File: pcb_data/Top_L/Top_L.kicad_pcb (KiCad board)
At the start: 2 copper layers, 158.4 x 96.4 mm, 75 parts, among them U1 XIAO-nRF52840

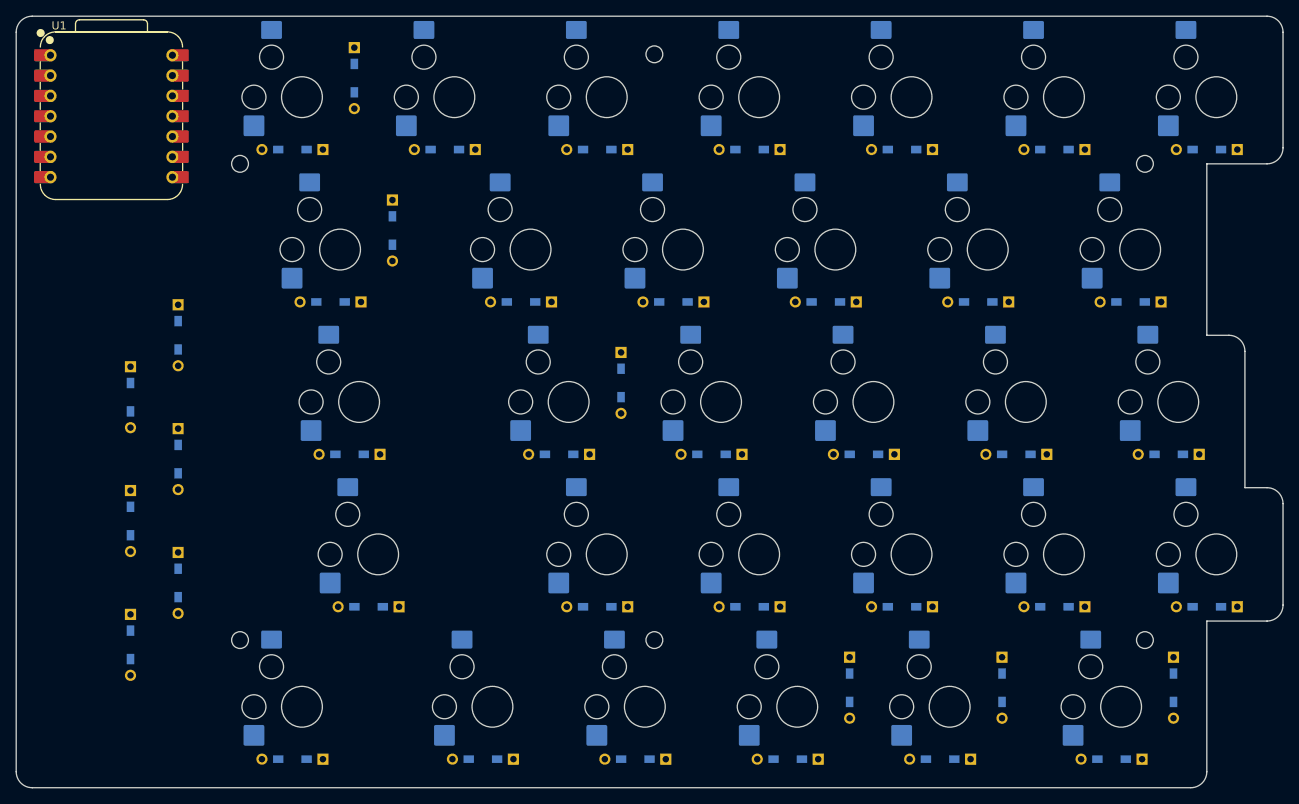
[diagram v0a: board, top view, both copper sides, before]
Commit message: remove diode
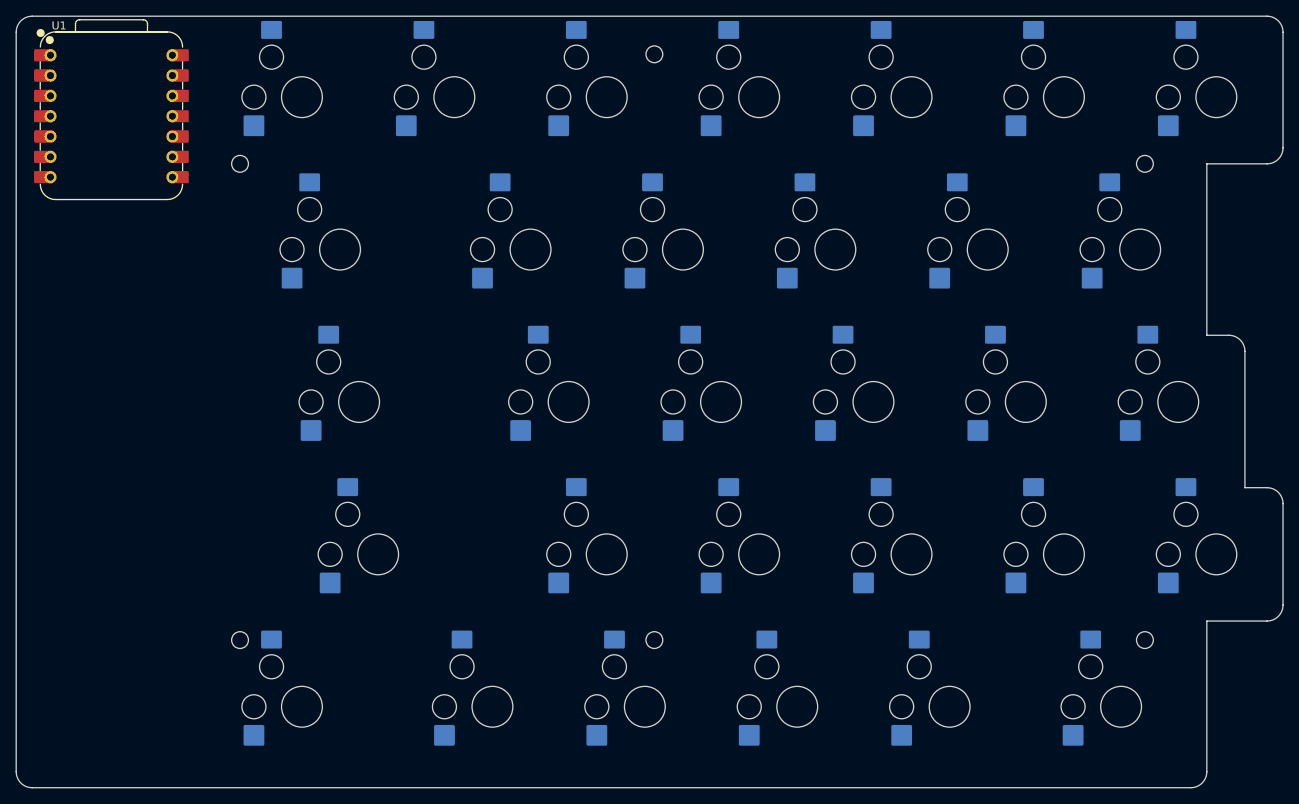
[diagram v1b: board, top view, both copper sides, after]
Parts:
- removed D0-1, D0-2, D0-3, D0-4, D1-0, D1-2, D1-3, D1-4, D2-0, D2-1, D2-3, D2-4, D3-0, D3-1, D3-2, D3-4, D4-0, D4-1, D4-2, D4-3, D5-0, D5-1, D5-2, D5-3, D5-4, D6-0, D6-1, D6-2, D6-3, D6-4, D6-5, DI0, DI1, DI2, DI3, DI4, DI5, DS0, DS1, DS2, DS3, DS4, DS5: 1N4148W, kbd_Parts:Diode_TH_SMD

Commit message: replace fp
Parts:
- RC0-1: footprint custom-library:Kailh-PG1353-Hotswap-L-1.5U -> kbd_SW_Hole:SW_Hole_1.5u
- RC0-2: footprint custom-library:Kailh-PG1353-Hotswap-L-1.75U -> kbd_SW_Hole:SW_Hole_1.75u
- RC0-3: footprint custom-library:Kailh-PG1353-Hotswap-L-2U -> kbd_SW_Hole:SW_Hole_2u
- RC6-5: footprint custom-library:Kailh-PG1353-Hotswap-L-1.25U -> kbd_SW_Hole:SW_Hole_1.25u
- turned RC0-3 to 180 degrees

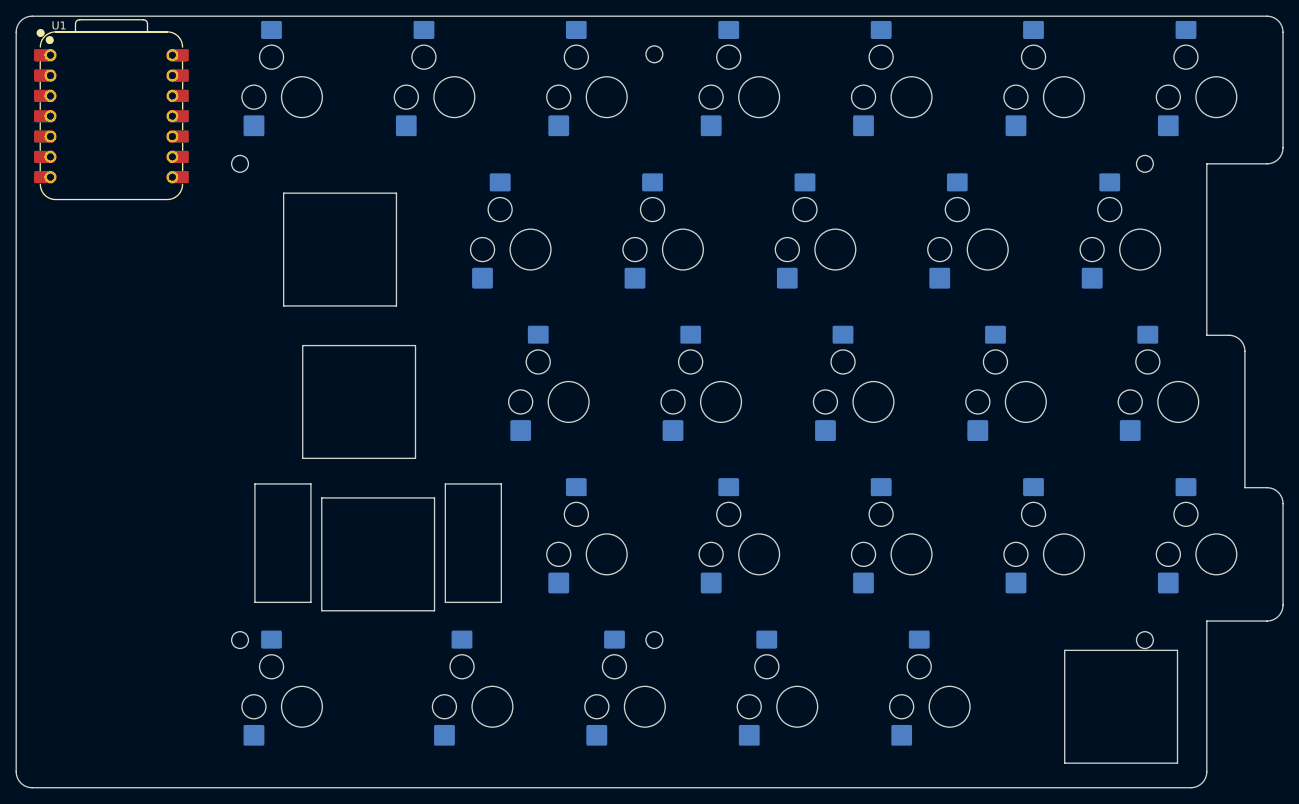
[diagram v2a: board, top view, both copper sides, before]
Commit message: replace fp
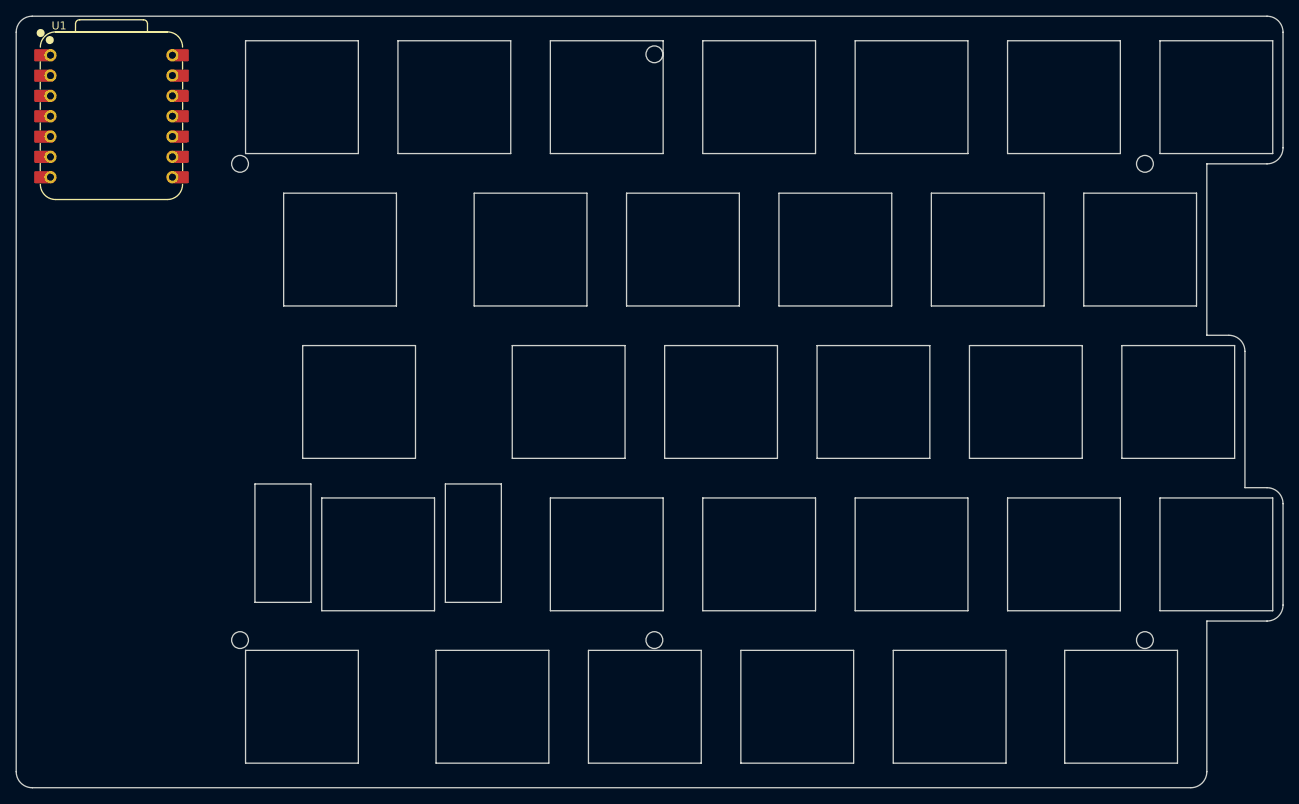
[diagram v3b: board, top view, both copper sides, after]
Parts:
- RC0-4, RC1-0, RC1-2, RC1-3, RC1-4, RC2-0, RC2-1, RC2-3, RC2-4, RC3-0, RC3-1, RC3-2, RC3-4, RC4-0, RC4-1, RC4-2, RC4-3, RC5-0, RC5-1, RC5-2, RC5-3, RC5-4, RC6-0, RC6-1, RC6-2, RC6-3, RC6-4: footprint custom-library:Kailh-PG1353-Hotswap-L-1U -> kbd_SW_Hole:SW_Hole_1u

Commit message: replace fp (m2 screw hole)
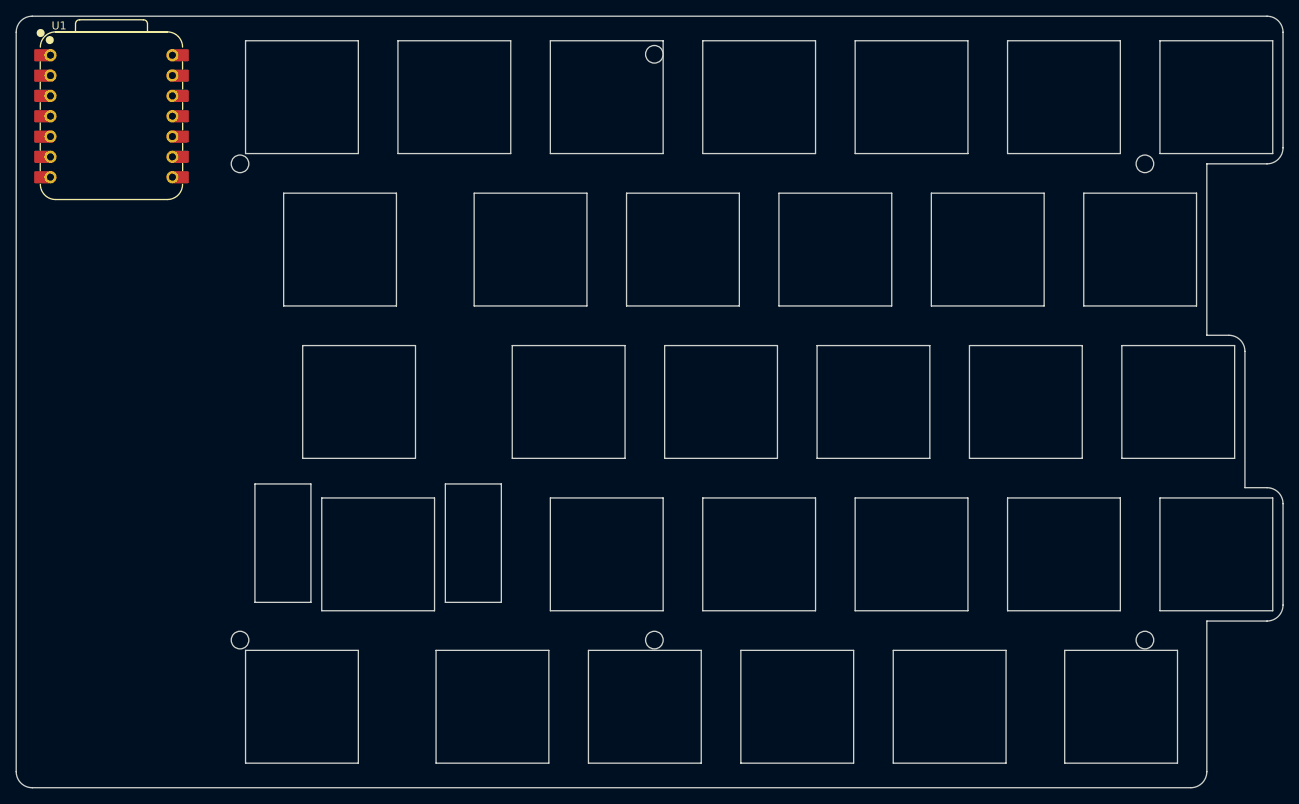
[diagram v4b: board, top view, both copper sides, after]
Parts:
- added Ref**: Val**, kbd_Hole:m2_Screw_Hole, F.Cu at (125.0, 125.0)
- added Ref**: Val**, kbd_Hole:m2_Screw_Hole, F.Cu at (125.0, 51.8)
- added Ref**: Val**, kbd_Hole:m2_Screw_Hole, F.Cu at (186.3, 65.5)
- added Ref**: Val**, kbd_Hole:m2_Screw_Hole, F.Cu at (186.3, 125.0)
- added Ref**: Val**, kbd_Hole:m2_Screw_Hole, F.Cu at (73.2, 125.0)
- added Ref**: Val**, kbd_Hole:m2_Screw_Hole, F.Cu at (73.2, 65.5)
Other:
- outline, holes or cut-outs redrawn
